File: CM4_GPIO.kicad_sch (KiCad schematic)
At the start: 10 parts, among them U10 PUSB3FR4, U12 SI-51005-F, U9 PUSB3FR4

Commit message: Redid traces with correct requirements, needs double checking.
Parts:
- added D1: LED Green, LED_SMD:LED_0603_1608Metric, symbol Device:LED
- added R8: 1k, Resistor_SMD:R_0402_1005Metric_Pad0.72x0.64mm_HandSolder, symbol Device:R
- added TP1: TestPoint, TestPoint:TestPoint_Pad_2.0x2.0mm, symbol Connector:TestPoint
- U12: footprint SI-51005-F:BEL_SI-51005-F -> lib:BEL_SI-51005-F
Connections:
- net +3.3v: now also D1.2 (A)
- net nEXTRST: no longer names the net of Module1.100 (nEXTRST)
- net nEXTRST: now also R8.1
- new net: D1.1 (K), R8.2, TP1.1

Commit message: Adjusted 3.3v for CM4 3.3v output, PCIe stayed the same.
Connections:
- net +3.3v is gone; now on net 3.3V OUT (CM4.86): D1.2 (A), D3.2 (A), R7.2, U12.14 (LEDR_A), U12.16 (LEDL_A)
- net 3.3V OUT (CM4.84) is gone; now on net 3.3V OUT (CM4.86): Module1.84 (+3.3v_(Output))
- net 3.3V OUT (CM4.86): now also Module1.78 (GPIO_VREF(1.8v/3.3v_Input))
- net 1.8V OUT (CM4.88): no longer names the net of Module1.88 (+1.8v_(Output))
- net 1.8V OUT (CM4.90): no longer names the net of Module1.90 (+1.8v_(Output))
- no-connect marks 23 -> 24
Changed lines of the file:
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@@
+	)
+	(junction
+		(at 39.37 129.54)
+		(diameter 0)
+		(color 0 0 0 0)
 	)
 	(junction
@@
 	)
 	(no_connect
-		(at 48.26 121.92)
-	)
-	(no_connect
 		(at 109.22 111.76)
 	)
@@
 	)
 	(no_connect
+		(at 48.26 137.16)
+	)
+	(no_connect
 		(at 48.26 142.24)
 	)
@@
 	(no_connect
 		(at 109.22 96.52)
+	)
+	(no_connect
+		(at 48.26 134.62)
 	)
 	(no_connect
@@
 	(wire
 		(pts
+			(xy 12.7 140.97) (xy 20.32 140.97)
+		)
+		(stroke
+			(width 0)
+			(type default)
+		)
+	)
+	(wire
+		(pts
 			(xy 233.68 59.69) (xy 233.68 74.93)
 		)
@@
 	(wire
 		(pts
+			(xy 39.37 132.08) (xy 39.37 129.54)
+		)
+		(stroke
+			(width 0)
+			(type default)
+		)
+	)
+	(wire
+		(pts
 			(xy 195.58 39.37) (xy 207.01 39.37)
 		)
@@
 	(wire
 		(pts
-			(xy 41.91 132.08) (xy 48.26 132.08)
-		)
-		(stroke
-			(width 0)
-			(type default)
-		)
-	)
-	(wire
-		(pts
 			(xy 209.55 55.88) (xy 212.09 55.88)
 		)
@@
 	(wire
 		(pts
+			(xy 48.26 132.08) (xy 39.37 132.08)
+		)
+		(stroke
+			(width 0)
+			(type default)
+		)
+	)
+	(wire
+		(pts
 			(xy 44.45 96.52) (xy 48.26 96.52)
 		)
@@
 	(wire
 		(pts
-			(xy 41.91 134.62) (xy 48.26 134.62)
-		)
-		(stroke
-			(width 0)
-			(type default)
-		)
-	)
-	(wire
-		(pts
 			(xy 111.76 91.44) (xy 111.76 99.06)
 		)
@@
 	(wire
 		(pts
-			(xy 41.91 137.16) (xy 48.26 137.16)
-		)
-		(stroke
-			(width 0)
-			(type default)
-		)
-	)
-	(wire
-		(pts
 			(xy 233.68 59.69) (xy 234.95 59.69)
 		)
@@
 	(wire
 		(pts
+			(xy 48.26 121.92) (xy 39.37 121.92)
+		)
+		(stroke
+			(width 0)
+			(type default)
+		)
+	)
+	(wire
+		(pts
 			(xy 109.22 99.06) (xy 111.76 99.06)
 		)
@@
 	(wire
 		(pts
-			(xy 41.91 129.54) (xy 48.26 129.54)
+			(xy 39.37 129.54) (xy 48.26 129.54)
 		)
 		(stroke
@@
 	(wire
 		(pts
+			(xy 39.37 121.92) (xy 39.37 129.54)
+		)
+		(stroke
+			(width 0)
+			(type default)
+		)
+	)
+	(wire
+		(pts
 			(xy 222.25 29.21) (xy 234.95 29.21)
 		)
@@
 		(pts
 			(xy 212.09 55.88) (xy 212.09 57.15)
+		)
+		(stroke
+			(width 0)
+			(type default)
+		)
+	)
+	(wire
+		(pts
+			(xy 38.1 129.54) (xy 39.37 129.54)
 		)
 		(stroke
@@
 		)
 	)
+	(label "3.3V OUT (CM4.86)"
+		(at 13.97 140.97 0)
+		(effects
+			(font
+				(size 1.27 1.27)
+			)
+			(justify left bottom)
+		)
+	)
 	(label "TRD1_P"
 		(at 38.1 30.48 0)
@@
 			)
 			(justify left bottom)
-		)
-	)
-	(global_label "3.3V OUT (CM4.86)"
-		(shape output)
-		(at 41.91 132.08 180)
-		(fields_autoplaced yes)
-		(effects
-			(font
-				(size 1.27 1.27)
-			)
-			(justify right)
-		)
-		(property "Intersheetrefs" "${INTERSHEET_REFS}"
-			(at 20.6005 132.08 0)
-			(effects
-				(font
-					(size 1.27 1.27)
-				)
-				(justify right)
-				(hide yes)
-			)
-		)
-	)
-	(global_label "1.8V OUT (CM4.88)"
-		(shape output)
-		(at 41.91 134.62 180)
-		(fields_autoplaced yes)
-		(effects
-			(font
-				(size 1.27 1.27)
-			)
-			(justify right)
-		)
-		(property "Intersheetrefs" "${INTERSHEET_REFS}"
-			(at 20.6005 134.62 0)
-			(effects
-				(font
-					(size 1.27 1.27)
-				)
-				(justify right)
-				(hide yes)
-			)
-		)
-	)
-	(global_label "1.8V OUT (CM4.90)"
-		(shape output)
-		(at 41.91 137.16 180)
-		(fields_autoplaced yes)
-		(effects
-			(font
-				(size 1.27 1.27)
-			)
-			(justify right)
-		)
-		(property "Intersheetrefs" "${INTERSHEET_REFS}"
-			(at 20.6005 137.16 0)
-			(effects
-				(font
-					(size 1.27 1.27)
-				)
-				(justify right)
-				(hide yes)
-			)
-		)
-	)
-	(global_label "3.3V OUT (CM4.84)"
-		(shape output)
-		(at 41.91 129.54 180)
-		(fields_autoplaced yes)
-		(effects
-			(font
-				(size 1.27 1.27)
-			)
-			(justify right)
-		)
-		(property "Intersheetrefs" "${INTERSHEET_REFS}"
-			(at 20.6005 129.54 0)
-			(effects
-				(font
-					(size 1.27 1.27)
-				)
-				(justify right)
-				(hide yes)
-			)
 		)
 	)
@@
 		)
 	)
-	(hierarchical_label "+3.3v"
+	(hierarchical_label "3.3V OUT (CM4.86)"
 		(shape input)
 		(at 229.87 78.74 180)
@@
 		)
 	)
-	(hierarchical_label "+3.3v"
+	(hierarchical_label "3.3V OUT (CM4.86)"
 		(shape input)
 		(at 132.08 29.21 0)
@@
 		)
 	)
+	(hierarchical_label "3.3V OUT (CM4.86)"
+		(shape output)
+		(at 38.1 129.54 180)
+		(effects
+			(font
+				(size 1.27 1.27)
+			)
+			(justify right)
+		)
+	)
 	(hierarchical_label "+5v"
 		(shape input)
@@
 		)
 	)
-	(hierarchical_label "+3.3v"
+	(hierarchical_label "3.3V OUT (CM4.86)"
 		(shape input)
-		(at 20.32 140.97 180)
+		(at 12.7 140.97 180)
 		(effects
 			(font
@@
 		)
 	)
-	(hierarchical_label "+3.3v"
+	(hierarchical_label "3.3V OUT (CM4.86)"
 		(shape input)
 		(at 34.29 48.26 180)

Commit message: Hehe, smol board now
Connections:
- net 3.3V OUT (CM4.86): now also R7.1; no longer R7.2
- net at Module1.20 (EEPROM_nWP): now also R7.2; no longer R7.1
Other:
- moved on the sheet: D1, D3, R23, R7, R8, TP1, U12

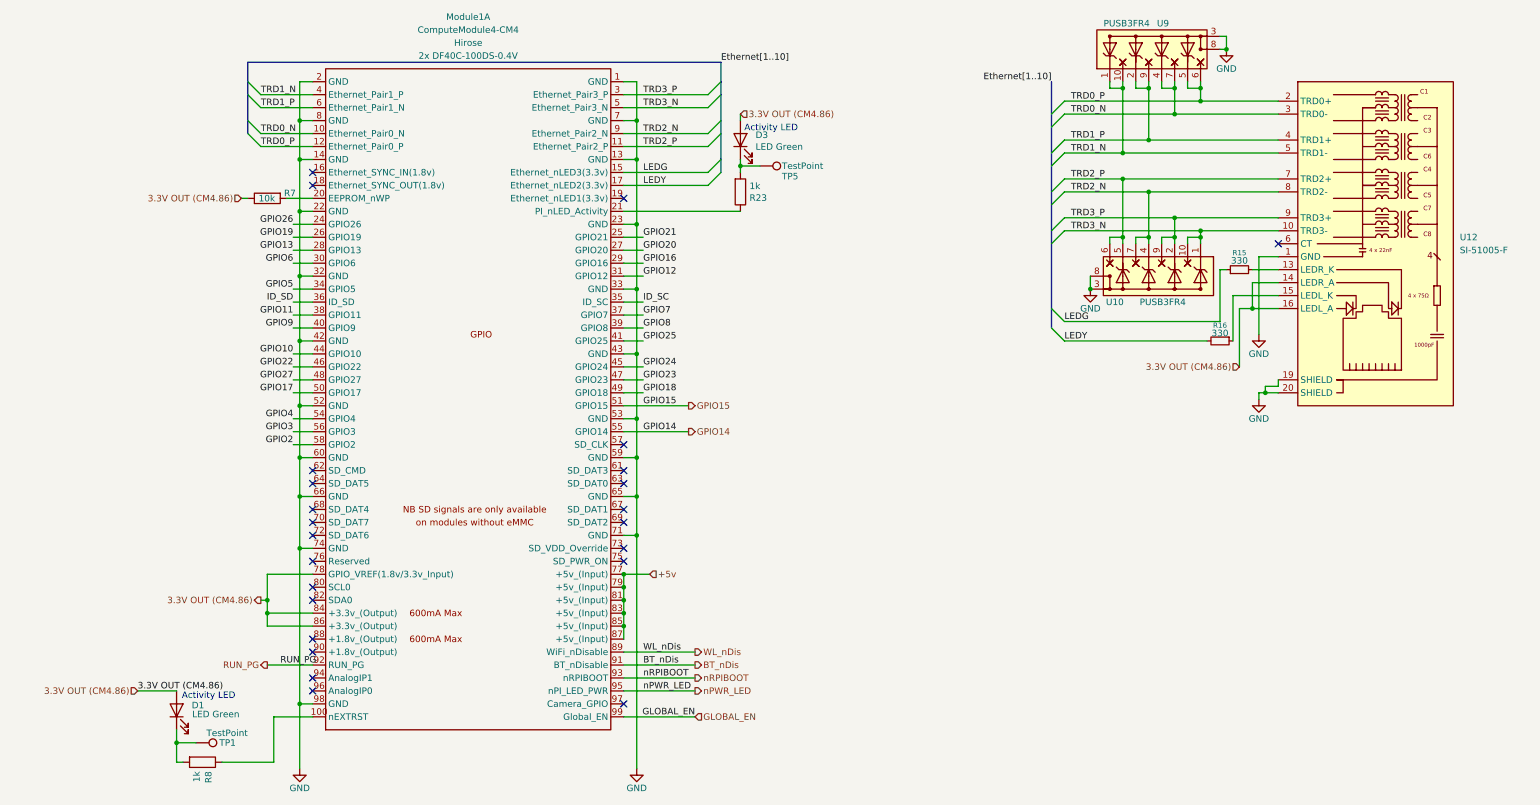
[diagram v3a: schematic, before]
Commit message: Changed quite a bit, PCB smoll now
Redid all traces, replaced HUSB238 with ch224k, made PCB even smaller.
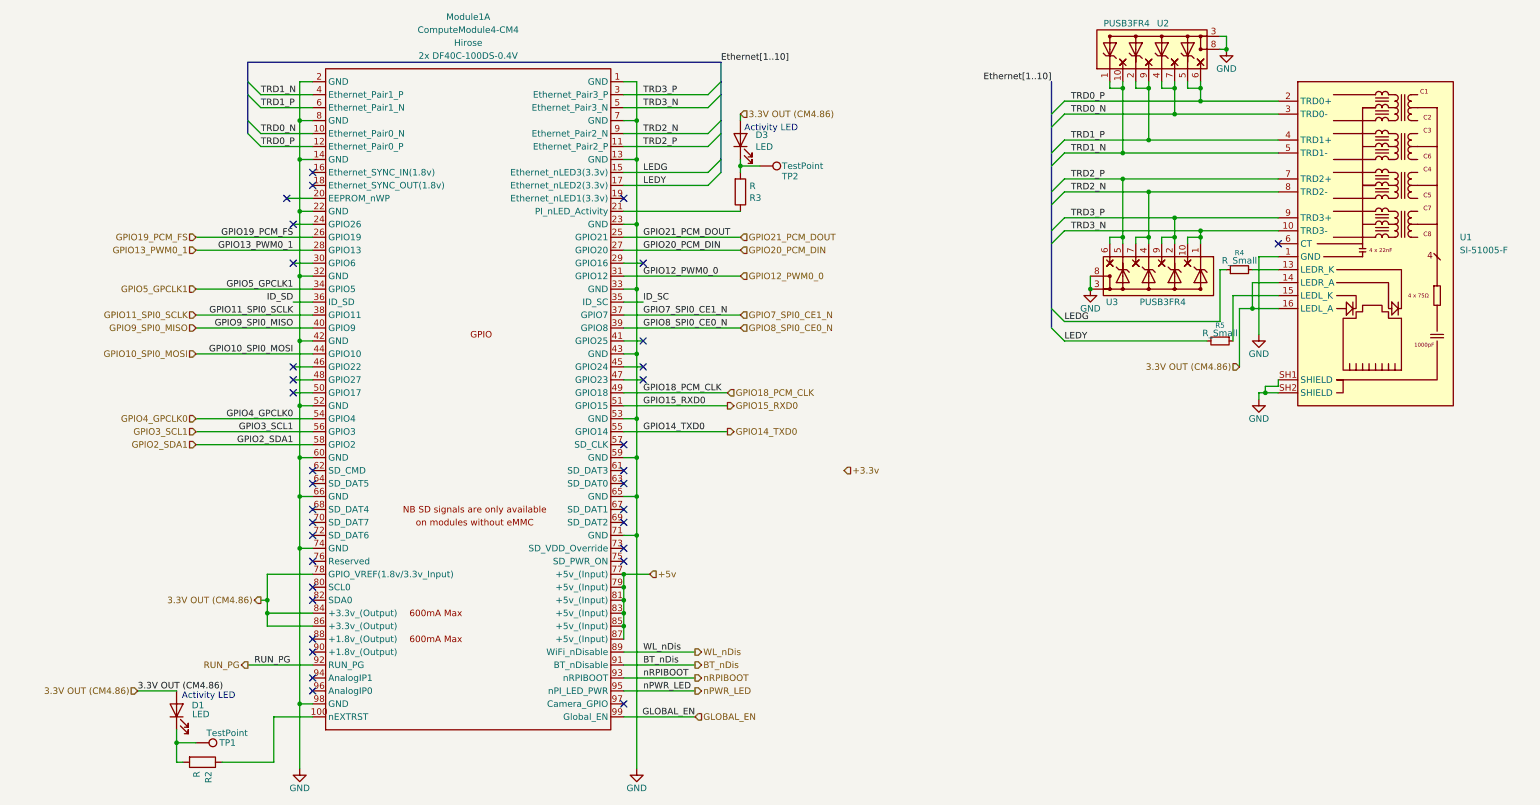
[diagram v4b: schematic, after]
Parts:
- removed R7: 10k, Resistor_SMD:R_0402_1005Metric_Pad0.72x0.64mm_HandSolder, symbol Device:R
- D1, D3: value LED Green -> LED
- Module1: footprint ComputeModule4:Raspberry-Pi-4-Compute-Module -> CM4IO:Raspberry-Pi-4-Compute-Module
- R2: renamed from R8; value 1k -> R
- R3: renamed from R23; value 1k -> R
- R4: renamed from R15; value 330 -> R_Small
- R5: renamed from R16; value 330 -> R_Small
- renumbered TP5 to TP2, U12 to U1, U9 to U2, U10 to U3
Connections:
- net GND: now also U1.SH1 (SHIELD), U1.SH2 (SHIELD); no longer U1.19 (SHIELD), U1.20 (SHIELD)
- net GPIO10 renamed GPIO10_SPI0_MOSI
- net GPIO11 renamed GPIO11_SPI0_SCLK
- net GPIO12 renamed GPIO12_PWM0_0
- net GPIO13 renamed GPIO13_PWM0_1
- net GPIO14 renamed GPIO14_TXD0
- net GPIO15 renamed GPIO15_RXD0
- net GPIO16: no longer names the net of Module1.29 (GPIO16)
- net GPIO17: no longer names the net of Module1.50 (GPIO17)
- net GPIO18 renamed GPIO18_PCM_CLK
- net GPIO19 renamed GPIO19_PCM_FS
- net GPIO2 renamed GPIO2_SDA1
- net GPIO20 renamed GPIO20_PCM_DIN
- net GPIO21 renamed GPIO21_PCM_DOUT
- net GPIO22: no longer names the net of Module1.46 (GPIO22)
- net GPIO23: no longer names the net of Module1.47 (GPIO23)
- net GPIO24: no longer names the net of Module1.45 (GPIO24)
- net GPIO25: no longer names the net of Module1.41 (GPIO25)
- net GPIO26: no longer names the net of Module1.24 (GPIO26)
- net GPIO27: no longer names the net of Module1.48 (GPIO27)
- net GPIO3 renamed GPIO3_SCL1
- net GPIO4 renamed GPIO4_GPCLK0
- net GPIO5 renamed GPIO5_GPCLK1
- net GPIO6: no longer names the net of Module1.30 (GPIO6)
- net GPIO7 renamed GPIO7_SPI0_CE1_N
- net GPIO8 renamed GPIO8_SPI0_CE0_N
- net GPIO9 renamed GPIO9_SPI0_MISO
- no-connect marks 24 -> 34

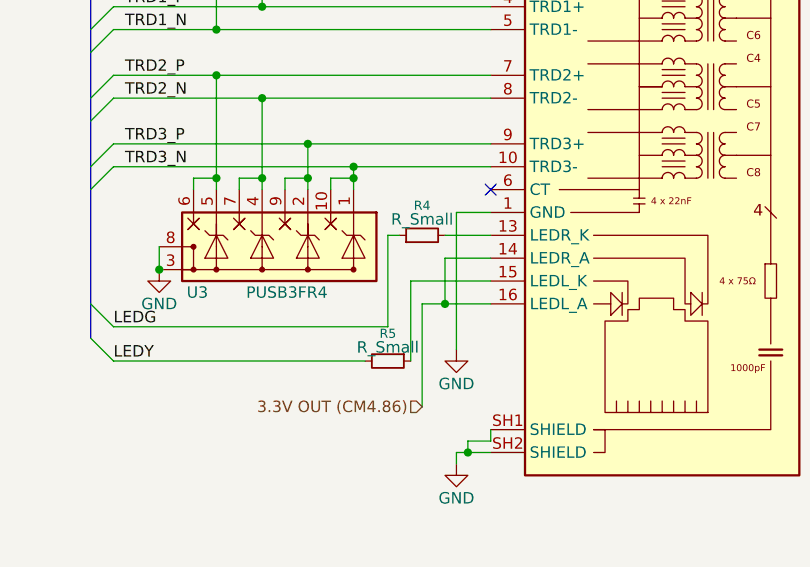
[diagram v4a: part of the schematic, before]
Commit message: Added datasheets for to-be-ordered components, double checked BOM
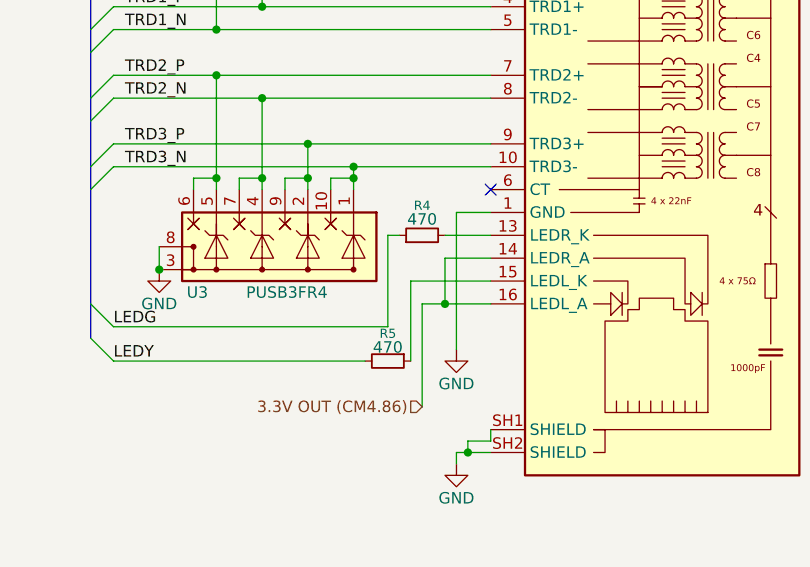
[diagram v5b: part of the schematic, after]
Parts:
- R4, R5: value R_Small -> 470
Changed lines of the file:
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@@
 			)
 		)
-		(property "Value" "R_Small"
+		(property "Value" "470"
 			(at 226.06 74.676 90)
 			(effects
@@
 			)
 		)
-		(property "Value" "R_Small"
+		(property "Value" "470"
 			(at 229.87 60.452 90)
 			(effects
